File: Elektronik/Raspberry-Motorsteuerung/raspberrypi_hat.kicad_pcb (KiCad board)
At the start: 4 copper layers, 65 x 56 mm, 32 parts, among them J1 Barrel_Jack_Switch, J10 Conn_01x02_Male, J11 Conn_01x02_Male, J15 Conn_01x02_Male, J2 Conn_01x04_Male, J3 40HAT, J6 Conn_01x04_Male, J8 Conn_01x02_Male, J9 CONN_01X02, Q1 DMG2305UX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

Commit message: improved barrel-jack/capacitor footprint and 12v lanes
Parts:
- removed REF**: OSHW-Logo2_9.8x8mm_SilkScreen, Symbol:OSHW-Logo2_9.8x8mm_SilkScreen
- C1: footprint SparkFun-Capacitors:CPOL-RADIAL-100UF-25V -> Capacitor_THT:CP_Radial_D6.3mm_P2.50mm; moved to F.Cu
- D1: value LED -> LED_RED
- D2: value LED -> LED_GREEN
- D3: value LED -> LED_YELLOW
- J1: footprint SparkFun-Connectors:POWER_JACK_PTH_BREAD -> Connector_BarrelJack:BarrelJack_Wuerth_6941xx301002
- moved J1 14.0 mm to (133.3, 102.6)
- moved C1 1.56 mm to (128.3, 105.0), turned to 180 degrees
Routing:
- net GND: track 176.4 -> 180.4 mm

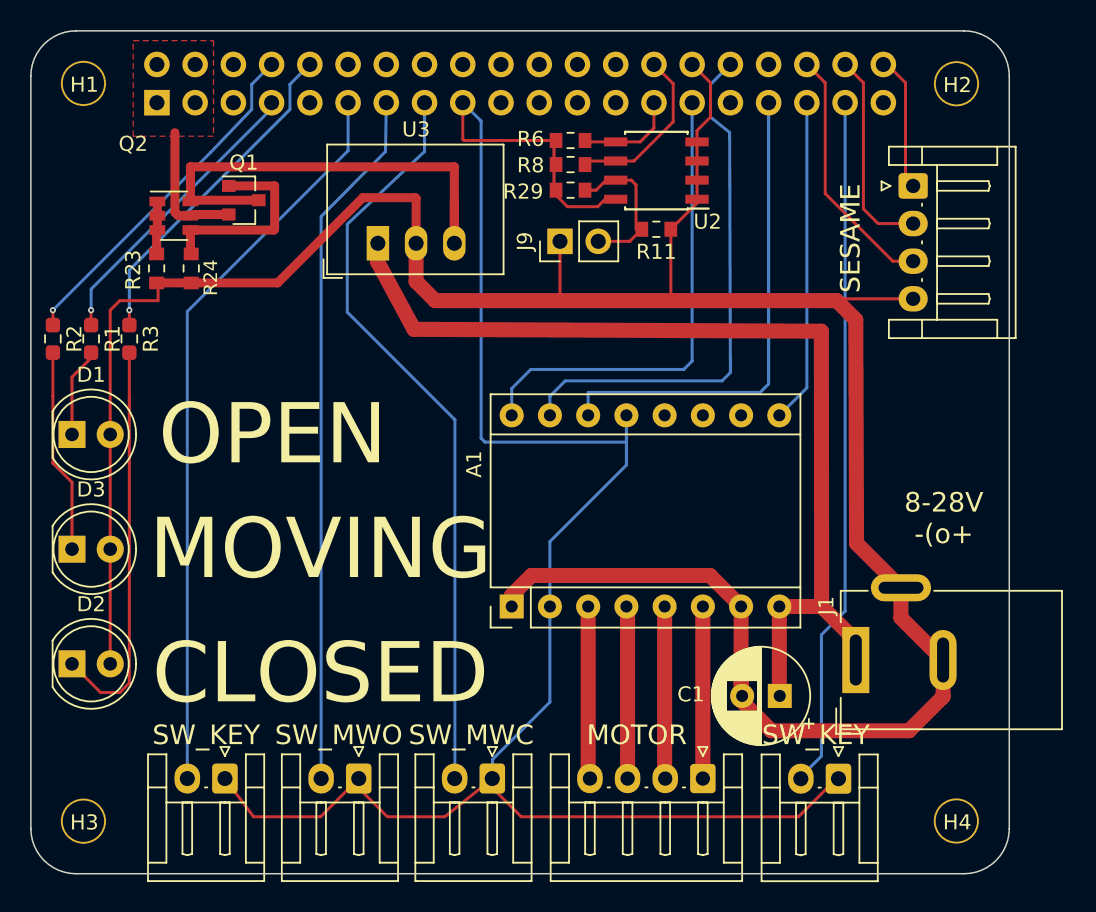
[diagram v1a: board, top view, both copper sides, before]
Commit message: changed to 2 layer board
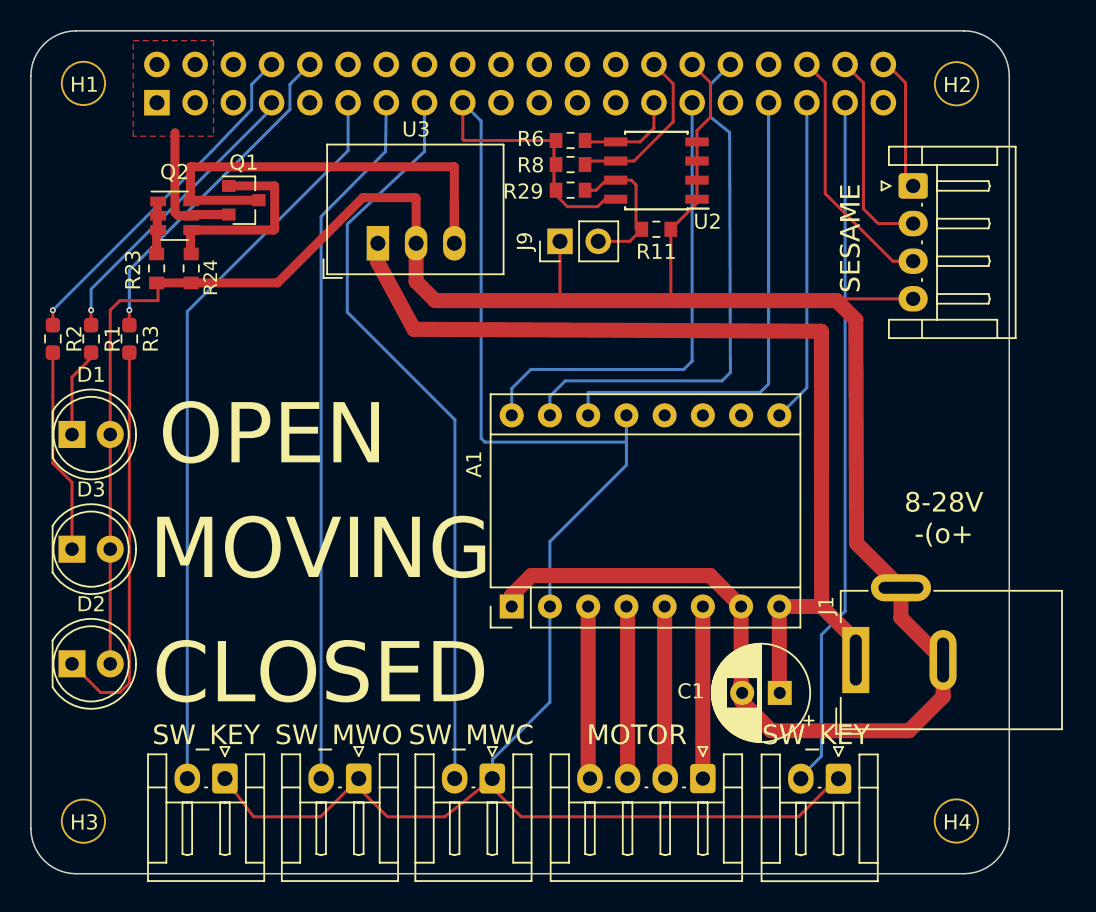
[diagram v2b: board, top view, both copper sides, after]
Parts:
- moved C1 0.20 mm to (128.3, 104.8)
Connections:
- C1 pad 1: (no net) -> /P12V
- C1 pad 2: (no net) -> GND
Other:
- copper layers 4 -> 2
